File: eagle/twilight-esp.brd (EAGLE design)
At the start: 87 x 37 mm, 16 parts, among them IC1 7805T, J1 Mini PIR, J2 VOUT, J3 VIN, Q1 IRF540

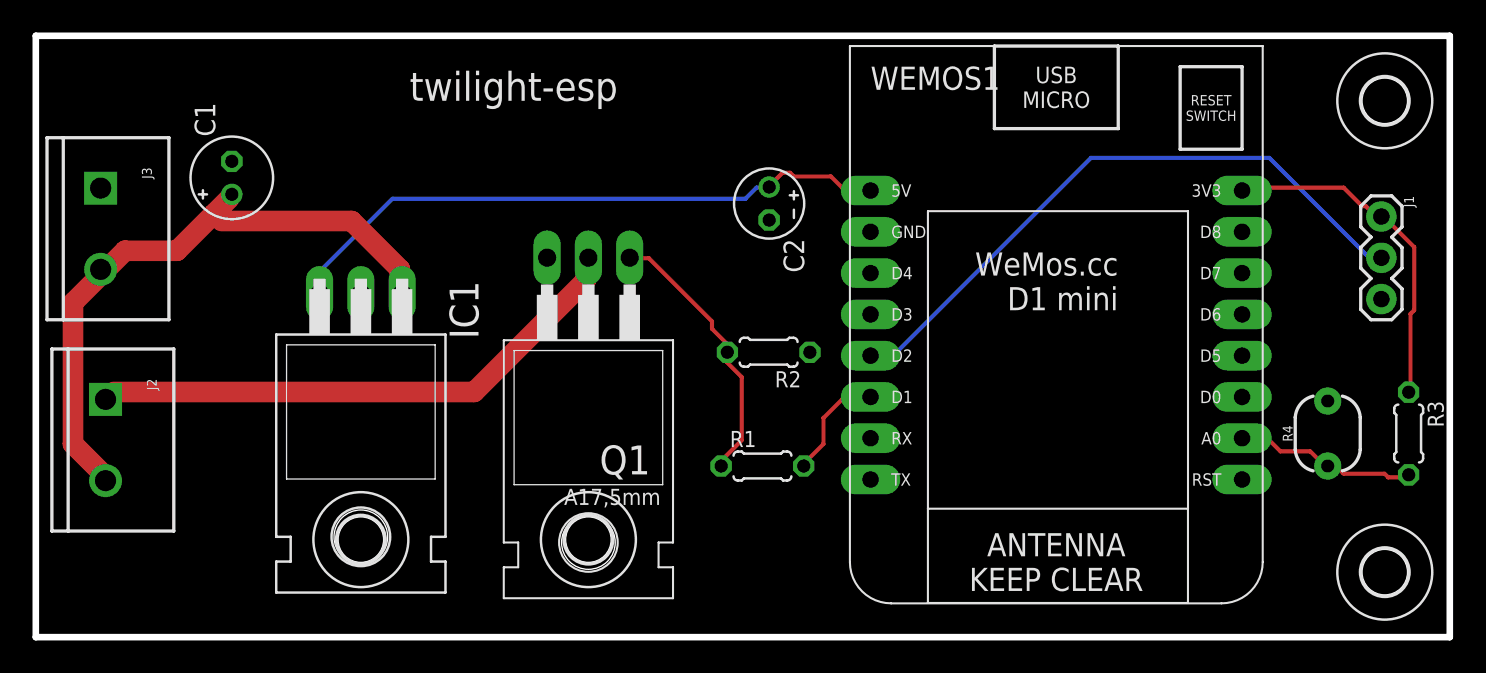
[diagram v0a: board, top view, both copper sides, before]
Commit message: add start state; flash pir led
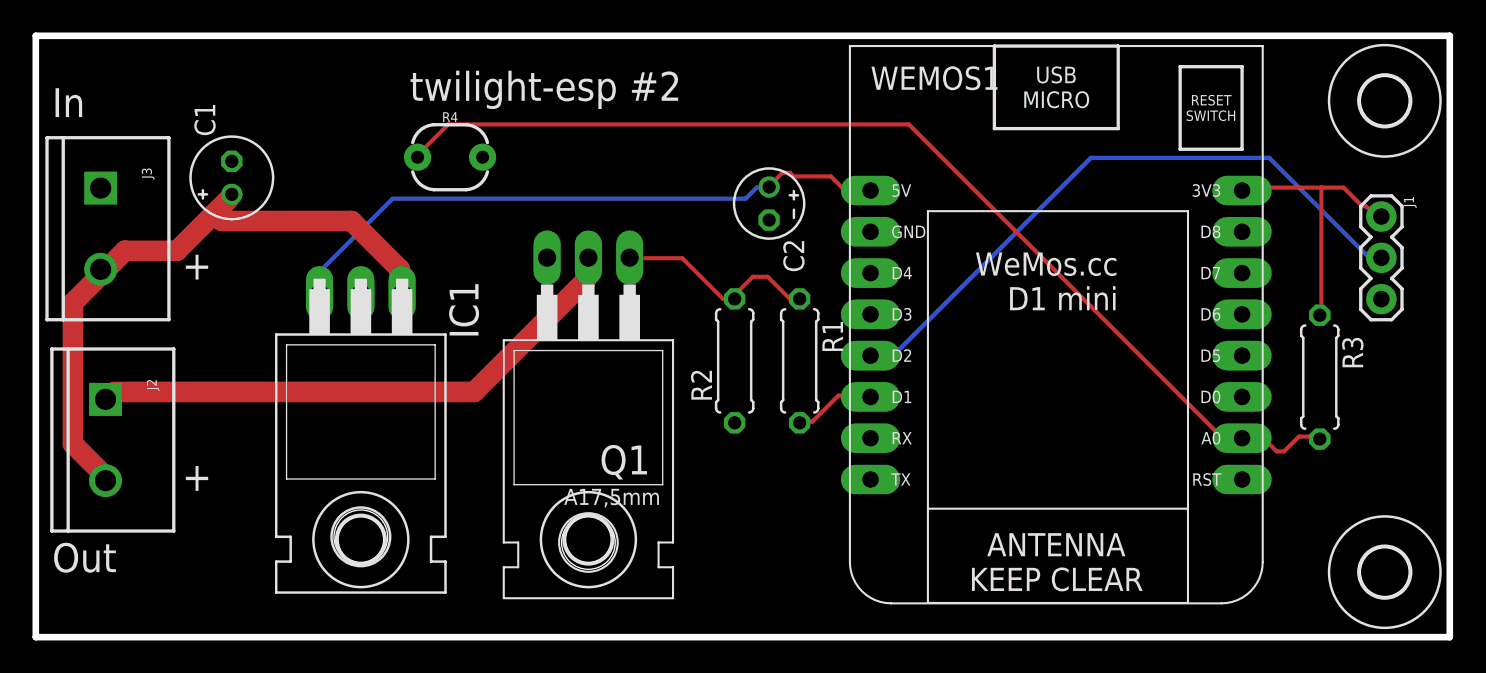
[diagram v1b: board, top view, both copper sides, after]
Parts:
- R1, R2, R3: device resistor:0204/5 -> rcl:0207/7
- U$3, U$4: device holes:2,8 -> holes:3,0
- moved R4 56.6 mm to (25.5, 29.5), turned to 0 degrees
- moved U$3 29.0 mm to (83.0, 33.0)
- moved U$4 29.0 mm to (83.0, 4.00)
- moved R1 6.86 mm to (47.0, 17.0), turned to 270 degrees
- moved R3 6.48 mm to (79.0, 16.0)
- moved R2 2.16 mm to (43.0, 17.0), turned to 90 degrees
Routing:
- net N$3: track 11.4 -> 65.2 mm
- net N$2: track 16.9 -> 12.8 mm
- net 3.3V: track 21.4 -> 17.4 mm
- net N$1: track 6.87 -> 5.06 mm
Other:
- board text added: "(c) 2018 steve"
- board text added: "+"
- board text added: "In"
- board text added: "Out"
- board text added: "twilight-esp #2"
- board text removed: "(c) 2017 steve"
- board text removed: "twilight-esp"
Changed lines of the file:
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@@
 <wire x1="87" y1="37" x2="0" y2="37" width="0.4064" layer="20"/>
 <wire x1="0" y1="37" x2="0" y2="0" width="0.4064" layer="20"/>
-<text x="23" y="33" size="1.778" layer="21">twilight-esp</text>
-<text x="38" y="33" size="1.778" layer="22" rot="MR0">(c) 2017 steve</text>
+<text x="23" y="33" size="1.778" layer="21">twilight-esp #2</text>
+<text x="38" y="33" size="1.778" layer="22" rot="MR0">(c) 2018 steve</text>
+<text x="1" y="32" size="1.778" layer="21">In</text>
+<text x="1" y="4" size="1.778" layer="21">Out</text>
+<text x="9" y="9" size="1.778" layer="21">+</text>
+<text x="9" y="22" size="1.778" layer="21">+</text>
 </plain>
 <attributes>
@@
 <attribute name="SF_SKU" value="PRT-08432" x="3.99" y="27.63" size="1.778" layer="27" rot="R270" display="off"/>
 </element>
-<element name="R1" library="resistor" package="0204/5" value="1k" x="44.71" y="10.53"/>
-<element name="R2" library="resistor" package="0204/5" value="47k" x="45.09" y="17.53" rot="R180"/>
-<element name="R3" library="resistor" package="0204/5" value="22k" x="84.47" y="12.53" rot="R270"/>
-<element name="R4" library="SparkFun-Sensors" package="PHOTOCELL" value="10k" x="79.49" y="12.53" rot="R90">
-<attribute name="PROD_ID" value="COMP-09129" x="79.49" y="12.53" size="1.778" layer="27" rot="R90" display="off"/>
-<attribute name="SF_ID" value="SEN-09088" x="79.49" y="12.53" size="1.778" layer="27" rot="R90" display="off"/>
+<element name="R4" library="SparkFun-Sensors" package="PHOTOCELL" value="10k" x="25.49" y="29.53">
+<attribute name="PROD_ID" value="COMP-09129" x="25.49" y="29.53" size="1.778" layer="27" display="off"/>
+<attribute name="SF_ID" value="SEN-09088" x="25.49" y="29.53" size="1.778" layer="27" display="off"/>
 </element>
 <element name="WEMOS1" library="esp8266modules" package="WEMOS-D1-MINI" value="Mini D1" x="64.06" y="17.32" rot="R180"/>
@@
 <element name="U$1" library="holes" package="2,8" value="" x="20" y="6"/>
 <element name="U$2" library="holes" package="2,8" value="" x="34" y="6"/>
-<element name="U$3" library="holes" package="2,8" value="" x="83" y="4"/>
-<element name="U$4" library="holes" package="2,8" value="" x="83" y="33"/>
+<element name="R1" library="rcl" package="0207/7" value="1k" x="47" y="17" rot="R270"/>
+<element name="R2" library="rcl" package="0207/7" value="47k" x="43" y="17" rot="R90"/>
+<element name="R3" library="rcl" package="0207/7" value="22k" x="79" y="16" rot="R270"/>
+<element name="U$3" library="holes" package="3,0" value="" x="83" y="33"/>
+<element name="U$4" library="holes" package="3,0" value="" x="83" y="4"/>
 </elements>
 <signals>
@@
 <contactref element="WEMOS1" pad="GND"/>
 <contactref element="J1" pad="3"/>
-<contactref element="R2" pad="1"/>
 <contactref element="R4" pad="2"/>
 <polygon width="0.4064" layer="16">
@@
 <vertex x="0" y="0"/>
 </polygon>
+<contactref element="R2" pad="1"/>
 </signal>
 <signal name="3.3V">
 <contactref element="J1" pad="1"/>
 <contactref element="WEMOS1" pad="3V3"/>
-<contactref element="R3" pad="1"/>
-<wire x1="84.582" y1="19.8882" x2="84.582" y2="15.0876" width="0.254" layer="1"/>
-<wire x1="84.8106" y1="20.1168" x2="84.582" y2="19.8882" width="0.254" layer="1"/>
-<wire x1="84.8106" y1="24.003" x2="84.8106" y2="20.1168" width="0.254" layer="1"/>
-<wire x1="82.9818" y1="25.8318" x2="84.8106" y2="24.003" width="0.254" layer="1"/>
-<wire x1="84.582" y1="15.0876" x2="84.47" y2="15.07" width="0.254" layer="1"/>
-<wire x1="82.9818" y1="25.8318" x2="82.79" y2="25.88" width="0.254" layer="1"/>
-<wire x1="80.4672" y1="27.6606" x2="74.295" y2="27.6606" width="0.254" layer="1"/>
+<wire x1="80.4672" y1="27.6606" x2="79.0956" y2="27.6606" width="0.254" layer="1"/>
+<wire x1="79.0956" y1="27.6606" x2="74.295" y2="27.6606" width="0.254" layer="1"/>
 <wire x1="81.6102" y1="26.5176" x2="80.4672" y2="27.6606" width="0.254" layer="1"/>
 <wire x1="81.8388" y1="26.5176" x2="81.6102" y2="26.5176" width="0.254" layer="1"/>
@@
 <wire x1="74.295" y1="27.6606" x2="74.22" y2="27.48" width="0.254" layer="1"/>
 <wire x1="82.7532" y1="26.0604" x2="82.79" y2="25.88" width="0.254" layer="1"/>
+<contactref element="R3" pad="1"/>
+<wire x1="79.0956" y1="27.6606" x2="79.0956" y2="19.8882" width="0.254" layer="1"/>
+<wire x1="79.0956" y1="19.8882" x2="79" y2="19.81" width="0.254" layer="1"/>
 </signal>
 <signal name="N$5">
@@
 </signal>
 <signal name="N$1">
+<contactref element="WEMOS1" pad="D1"/>
 <contactref element="R1" pad="2"/>
-<contactref element="WEMOS1" pad="D1"/>
-<wire x1="48.4632" y1="11.8872" x2="47.3202" y2="10.7442" width="0.254" layer="1"/>
-<wire x1="48.4632" y1="13.4874" x2="48.4632" y2="11.8872" width="0.254" layer="1"/>
-<wire x1="49.6062" y1="14.6304" x2="48.4632" y2="13.4874" width="0.254" layer="1"/>
-<wire x1="51.2064" y1="14.6304" x2="49.6062" y2="14.6304" width="0.254" layer="1"/>
-<wire x1="47.3202" y1="10.7442" x2="47.25" y2="10.53" width="0.254" layer="1"/>
-<wire x1="51.2064" y1="14.6304" x2="51.36" y2="14.78" width="0.254" layer="1"/>
+<wire x1="47.7774" y1="13.2588" x2="47.0916" y2="13.2588" width="0.254" layer="1"/>
+<wire x1="49.3776" y1="14.859" x2="47.7774" y2="13.2588" width="0.254" layer="1"/>
+<wire x1="51.2064" y1="14.859" x2="49.3776" y2="14.859" width="0.254" layer="1"/>
+<wire x1="47.0916" y1="13.2588" x2="47" y2="13.19" width="0.254" layer="1"/>
+<wire x1="51.2064" y1="14.859" x2="51.36" y2="14.78" width="0.254" layer="1"/>
 </signal>
 <signal name="N$2">
+<contactref element="Q1" pad="1"/>
 <contactref element="R1" pad="1"/>
 <contactref element="R2" pad="2"/>
-<contactref element="Q1" pad="1"/>
-<wire x1="42.291" y1="10.9728" x2="42.291" y2="10.7442" width="0.254" layer="1"/>
-<wire x1="43.434" y1="12.1158" x2="42.291" y2="10.9728" width="0.254" layer="1"/>
-<wire x1="43.434" y1="16.002" x2="43.434" y2="12.1158" width="0.254" layer="1"/>
-<wire x1="42.5196" y1="16.9164" x2="43.434" y2="16.002" width="0.254" layer="1"/>
-<wire x1="42.5196" y1="17.3736" x2="42.5196" y2="16.9164" width="0.254" layer="1"/>
-<wire x1="42.291" y1="10.7442" x2="42.17" y2="10.53" width="0.254" layer="1"/>
-<wire x1="42.5196" y1="17.3736" x2="42.55" y2="17.53" width="0.254" layer="1"/>
-<wire x1="37.719" y1="23.3172" x2="36.576" y2="23.3172" width="0.254" layer="1"/>
-<wire x1="41.6052" y1="19.431" x2="37.719" y2="23.3172" width="0.254" layer="1"/>
-<wire x1="41.6052" y1="18.9738" x2="41.6052" y2="19.431" width="0.254" layer="1"/>
-<wire x1="42.5196" y1="18.0594" x2="41.6052" y2="18.9738" width="0.254" layer="1"/>
-<wire x1="42.5196" y1="17.6022" x2="42.5196" y2="18.0594" width="0.254" layer="1"/>
+<wire x1="43.2054" y1="21.2598" x2="43.2054" y2="21.0312" width="0.254" layer="1"/>
+<wire x1="44.1198" y1="22.1742" x2="43.2054" y2="21.2598" width="0.254" layer="1"/>
+<wire x1="45.0342" y1="22.1742" x2="44.1198" y2="22.1742" width="0.254" layer="1"/>
+<wire x1="46.4058" y1="20.8026" x2="45.0342" y2="22.1742" width="0.254" layer="1"/>
+<wire x1="46.863" y1="20.8026" x2="46.4058" y2="20.8026" width="0.254" layer="1"/>
+<wire x1="43.2054" y1="21.0312" x2="43" y2="20.81" width="0.254" layer="1"/>
+<wire x1="46.863" y1="20.8026" x2="47" y2="20.81" width="0.254" layer="1"/>
+<wire x1="39.7764" y1="23.3172" x2="36.576" y2="23.3172" width="0.254" layer="1"/>
+<wire x1="42.291" y1="20.8026" x2="39.7764" y2="23.3172" width="0.254" layer="1"/>
+<wire x1="42.9768" y1="20.8026" x2="42.291" y2="20.8026" width="0.254" layer="1"/>
 <wire x1="36.576" y1="23.3172" x2="36.54" y2="23.35" width="0.254" layer="1"/>
-<wire x1="42.5196" y1="17.6022" x2="42.55" y2="17.53" width="0.254" layer="1"/>
+<wire x1="42.9768" y1="20.8026" x2="43" y2="20.81" width="0.254" layer="1"/>
 </signal>
 <signal name="N$8">
@@
 <signal name="N$3">
 <contactref element="R4" pad="1"/>
+<contactref element="WEMOS1" pad="A0"/>
 <contactref element="R3" pad="2"/>
-<contactref element="WEMOS1" pad="A0"/>
-<wire x1="83.2104" y1="9.8298" x2="84.3534" y2="9.8298" width="0.254" layer="1"/>
-<wire x1="82.9818" y1="10.0584" x2="83.2104" y2="9.8298" width="0.254" layer="1"/>
-<wire x1="80.4672" y1="10.0584" x2="82.9818" y2="10.0584" width="0.254" layer="1"/>
-<wire x1="80.01" y1="10.5156" x2="80.4672" y2="10.0584" width="0.254" layer="1"/>
-<wire x1="79.5528" y1="10.5156" x2="80.01" y2="10.5156" width="0.254" layer="1"/>
-<wire x1="84.3534" y1="9.8298" x2="84.47" y2="9.99" width="0.254" layer="1"/>
-<wire x1="79.5528" y1="10.5156" x2="79.49" y2="10.53" width="0.254" layer="1"/>
-<wire x1="75.8952" y1="12.1158" x2="74.295" y2="12.1158" width="0.254" layer="1"/>
-<wire x1="76.581" y1="11.43" x2="75.8952" y2="12.1158" width="0.254" layer="1"/>
-<wire x1="78.4098" y1="11.43" x2="76.581" y2="11.43" width="0.254" layer="1"/>
-<wire x1="79.3242" y1="10.5156" x2="78.4098" y2="11.43" width="0.254" layer="1"/>
+<wire x1="77.724" y1="12.3444" x2="78.867" y2="12.3444" width="0.254" layer="1"/>
+<wire x1="76.8096" y1="11.43" x2="77.724" y2="12.3444" width="0.254" layer="1"/>
+<wire x1="76.3524" y1="11.43" x2="76.8096" y2="11.43" width="0.254" layer="1"/>
+<wire x1="75.6666" y1="12.1158" x2="76.3524" y2="11.43" width="0.254" layer="1"/>
+<wire x1="74.295" y1="12.1158" x2="75.6666" y2="12.1158" width="0.254" layer="1"/>
+<wire x1="78.867" y1="12.3444" x2="79" y2="12.19" width="0.254" layer="1"/>
 <wire x1="74.295" y1="12.1158" x2="74.22" y2="12.24" width="0.254" layer="1"/>
-<wire x1="79.3242" y1="10.5156" x2="79.49" y2="10.53" width="0.254" layer="1"/>
+<wire x1="25.3746" y1="31.5468" x2="23.5458" y2="29.718" width="0.254" layer="1"/>
+<wire x1="53.721" y1="31.5468" x2="25.3746" y2="31.5468" width="0.254" layer="1"/>
+<wire x1="72.9234" y1="12.3444" x2="53.721" y2="31.5468" width="0.254" layer="1"/>
+<wire x1="74.0664" y1="12.3444" x2="72.9234" y2="12.3444" width="0.254" layer="1"/>
+<wire x1="23.5458" y1="29.718" x2="23.49" y2="29.53" width="0.254" layer="1"/>
+<wire x1="74.0664" y1="12.3444" x2="74.22" y2="12.24" width="0.254" layer="1"/>
 </signal>
 </signals>
+<errors>
+</errors>
 </board>
 </drawing>

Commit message: add reset header
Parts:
- added JP1: RESET, pinhead:1X02
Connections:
- new net N$4: JP1.1, WEMOS1.RESET
- net GND: now also JP1.2
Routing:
- net N$4: track 0.00 -> 29.0 mm
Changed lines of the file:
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@@
 <element name="U$3" library="holes" package="3,0" value="" x="83" y="33"/>
 <element name="U$4" library="holes" package="3,0" value="" x="83" y="4"/>
+<element name="JP1" library="pinhead" package="1X02" value="RESET" x="45" y="7" rot="R180"/>
 </elements>
 <signals>
@@
 </polygon>
 <contactref element="R2" pad="1"/>
+<contactref element="JP1" pad="2"/>
 </signal>
 <signal name="3.3V">
@@
 <wire x1="74.0664" y1="12.3444" x2="74.22" y2="12.24" width="0.254" layer="1"/>
 </signal>
+<signal name="N$4">
+<contactref element="WEMOS1" pad="RESET"/>
+<contactref element="JP1" pad="1"/>
+<wire x1="70.4088" y1="7.0866" x2="46.4058" y2="7.0866" width="0.254" layer="1"/>
+<wire x1="72.9234" y1="9.6012" x2="70.4088" y2="7.0866" width="0.254" layer="1"/>
+<wire x1="74.0664" y1="9.6012" x2="72.9234" y2="9.6012" width="0.254" layer="1"/>
+<wire x1="46.4058" y1="7.0866" x2="46.27" y2="7" width="0.254" layer="1"/>
+<wire x1="74.0664" y1="9.6012" x2="74.22" y2="9.7" width="0.254" layer="1"/>
+</signal>
 </signals>
